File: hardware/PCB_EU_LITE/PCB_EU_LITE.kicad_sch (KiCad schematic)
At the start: 0 parts

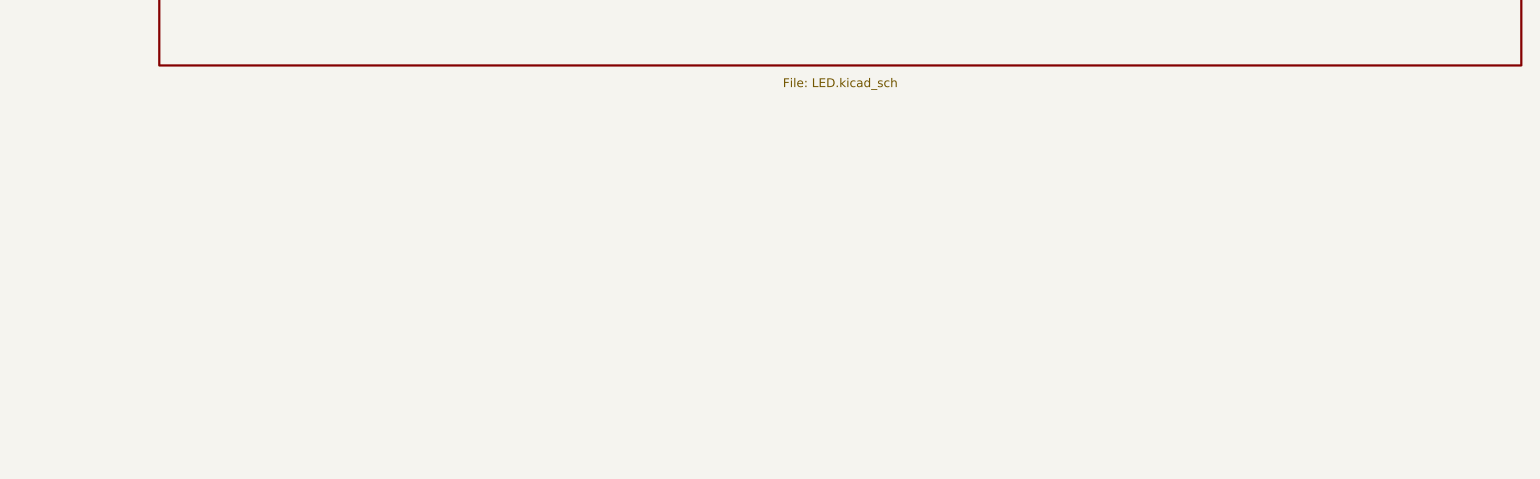
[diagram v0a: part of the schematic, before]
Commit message: Add RGB status LED to EU-LITE
Common-anode 5 mm RGB LED on +12V, three BC847B low-side switches driven from
GPIO4/16/17 (about 4.9/4.4/4.4 mA per channel, dark during reset). New
Status sheet, 56 script checks (5 more), 5 more mutation cases. The LED is in
neither the stock nor the catalogue snapshot: its BOM line has no price (the
estimate is stated separately). Docs carry a proposed status colour table; the
firmware is not changed.

Co-Authored-By: Claude <noreply@anthropic.com>
Claude-Session: https://claude.ai/code/session_013vgne5bRQcg5JyL7FL8xv5
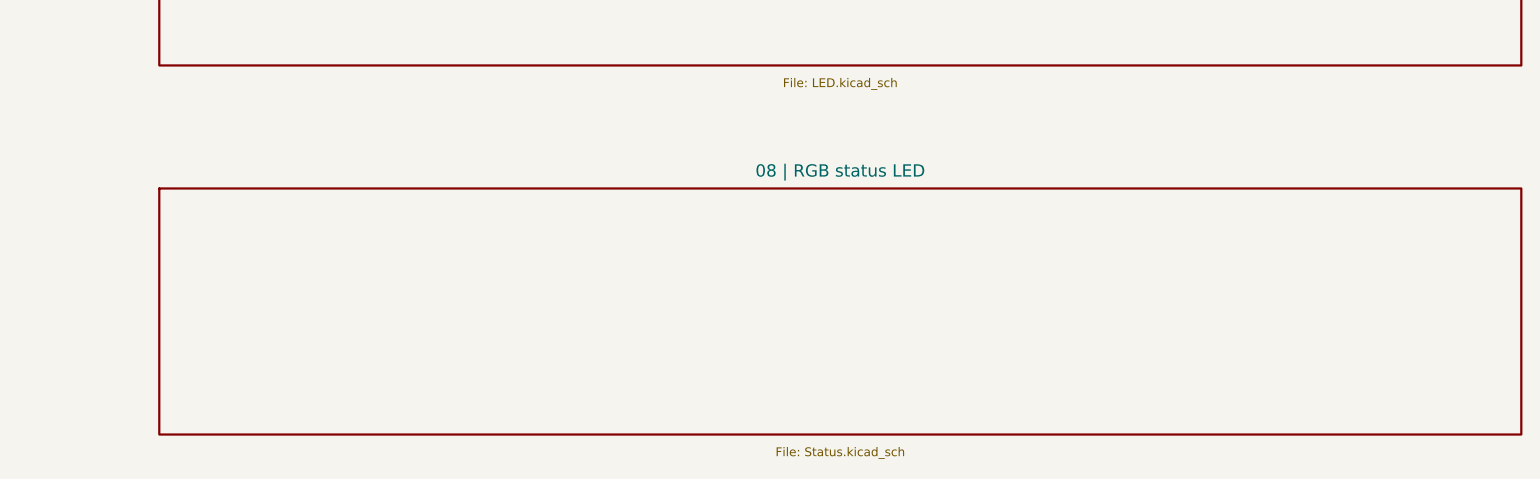
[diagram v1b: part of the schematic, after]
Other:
- added sheet 08 | RGB status LED (Status.kicad_sch)
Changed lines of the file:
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@@
 (sheet (at 210 159) (size 155 28) (stroke (width 0.254) (type default)) (fill (color 0 0 0 0)) (property "Sheetname" "06 | LED boost channel (LM3429, one channel)" (at 287.5 157 0) (effects (font (size 1.4 1.4)) )) (property "Sheetfile" "LED.kicad_sch" (at 287.5 189 0) (effects (font (size 1 1)) )) (instances (project "PCB_EU_LITE" (path "/6650c329-4f4f-5b7a-a019-ee8e8f2772e1" (page "7")))))
 (sheet (at 25 201) (size 155 28) (stroke (width 0.254) (type default)) (fill (color 0 0 0 0)) (property "Sheetname" "07 | PTC heater and 24 V pump" (at 102.5 199 0) (effects (font (size 1.4 1.4)) )) (property "Sheetfile" "Loads.kicad_sch" (at 102.5 231 0) (effects (font (size 1 1)) )) (instances (project "PCB_EU_LITE" (path "/6650c329-4f4f-5b7a-a019-ee8e8f2772e1" (page "8")))))
+(sheet (at 210 201) (size 155 28) (stroke (width 0.254) (type default)) (fill (color 0 0 0 0)) (property "Sheetname" "08 | RGB status LED" (at 287.5 199 0) (effects (font (size 1.4 1.4)) )) (property "Sheetfile" "Status.kicad_sch" (at 287.5 231 0) (effects (font (size 1 1)) )) (instances (project "PCB_EU_LITE" (path "/6650c329-4f4f-5b7a-a019-ee8e8f2772e1" (page "9")))))
 (sheet_instances (path "/" (page "1"))) (embedded_fonts no))
